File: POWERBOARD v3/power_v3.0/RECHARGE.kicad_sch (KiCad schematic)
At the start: 25 parts, among them J1 USB_C_Receptacle_USB2.0_16P, J2 B2B_PH_K_S, J3 R14 - 103AT-2, U2 BQ25886RGE

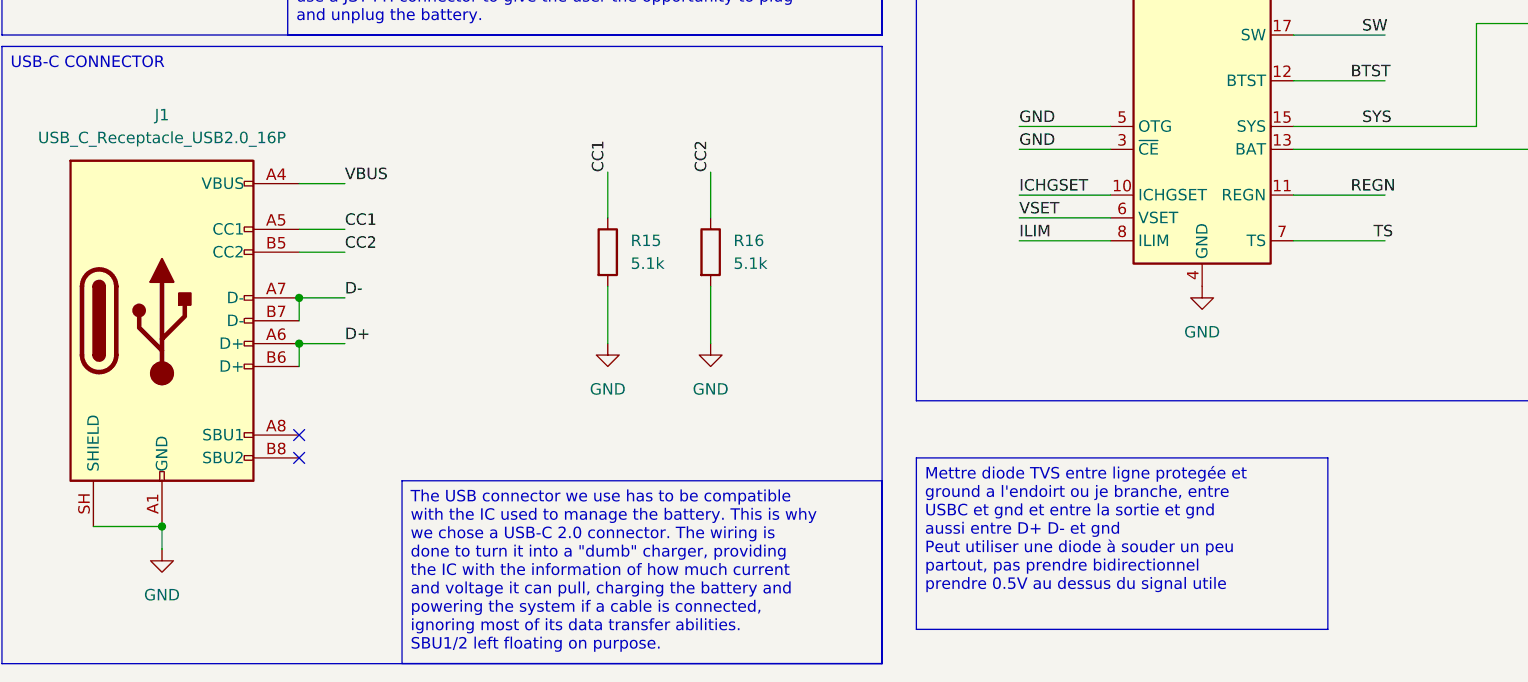
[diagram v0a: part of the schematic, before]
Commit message: added TVS diodes to charging circuit and (almost fully) routed 5.3 to 5V LDO
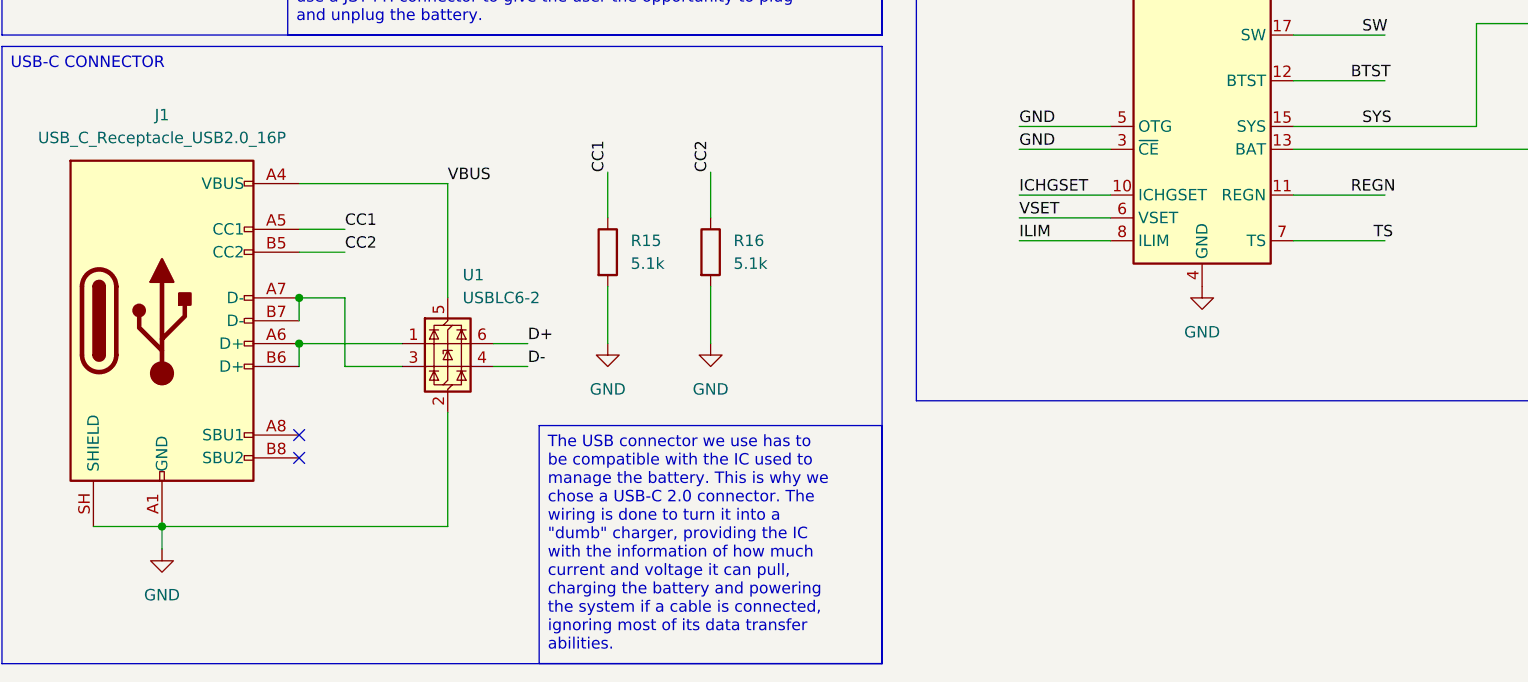
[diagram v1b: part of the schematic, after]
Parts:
- added U1: USBLC6-2, Package_TO_SOT_SMD:SOT-23-6, symbol Power_Protection:USBLC6-2SC6
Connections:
- net D+: now also U1.6 (I/O1); no longer J1.A6 (D+), J1.B6 (D+)
- net D-: now also U1.4 (I/O2); no longer J1.A7 (D-), J1.B7 (D-)
- net GND: now also U1.2 (GND)
- net VBUS: now also U1.5 (VBUS)
- new net: J1.A6 (D+), J1.B6 (D+), U1.1 (I/O1)
- new net: J1.A7 (D-), J1.B7 (D-), U1.3 (I/O2)
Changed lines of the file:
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@@
 		)
 	)
-	(text_box "Mettre diode TVS entre ligne protegée et ground a l'endoirt ou je branche, entre USBC et gnd et entre la sortie et gnd\naussi entre D+ D- et gnd\nPeut utiliser une diode à souder un peu partout, pas prendre bidirectionnel\nprendre 0.5V au dessus du signal utile"
-		(exclude_from_sim no)
-		(at 129.54 170.18 0)
-		(size 45.72 19.0501)
-		(margins 0.9525 0.9525 0.9525 0.9525)
-		(stroke
-			(width 0)
-			(type solid)
-		)
-		(fill
-			(type none)
-		)
-		(effects
-			(font
-				(size 1.27 1.27)
-			)
-			(justify left top)
-		)
-	)
 	(text_box "R14 is a thermistor to be placed as close to the battery as possible. The Seiko BMS integrated in our battery only handles the electric protection (charge, discharge) and not the temperature. Via TS, the IC progressively adjusts the charging profile according to the temperature to preserve the battery (JEITA). Its value at 25°C should be of 10kOhm."
 		(exclude_from_sim no)
@@
 		)
 	)
-	(text_box "The USB connector we use has to be compatible with the IC used to manage the battery. This is why we chose a USB-C 2.0 connector. The wiring is done to turn it into a \"dumb\" charger, providing the IC with the information of how much current and voltage it can pull, charging the battery and powering the system if a cable is connected, ignoring most of its data transfer abilities.\nSBU1/2 left floating on purpose."
+	(text_box "The USB connector we use has to be compatible with the IC used to manage the battery. This is why we chose a USB-C 2.0 connector. The wiring is done to turn it into a \"dumb\" charger, providing the IC with the information of how much current and voltage it can pull, charging the battery and powering the system if a cable is connected, ignoring most of its data transfer abilities."
 		(exclude_from_sim no)
-		(at 72.39 172.72 0)
-		(size 53.34 20.3053)
+		(at 87.63 166.5861 0)
+		(size 38.1 26.4392)
 		(margins 0.9525 0.9525 0.9525 0.9525)
 		(stroke
@@
 	(wire
 		(pts
+			(xy 82.55 157.48) (xy 86.36 157.48)
+		)
+		(stroke
+			(width 0)
+			(type default)
+		)
+	)
+	(wire
+		(pts
 			(xy 64.77 46.99) (xy 64.77 45.72)
 		)
@@
 	(wire
 		(pts
-			(xy 66.04 139.7) (xy 60.96 139.7)
+			(xy 60.96 139.7) (xy 77.47 139.7)
+		)
+		(stroke
+			(width 0)
+			(type default)
+		)
+	)
+	(wire
+		(pts
+			(xy 66.04 160.02) (xy 72.39 160.02)
 		)
 		(stroke
@@
 	(wire
 		(pts
-			(xy 60.96 157.48) (xy 66.04 157.48)
+			(xy 60.96 157.48) (xy 72.39 157.48)
 		)
 		(stroke
@@
 	(wire
 		(pts
+			(xy 82.55 160.02) (xy 86.36 160.02)
+		)
+		(stroke
+			(width 0)
+			(type default)
+		)
+	)
+	(wire
+		(pts
 			(xy 203.2 121.92) (xy 212.09 121.92)
 		)
@@
 	(wire
 		(pts
+			(xy 66.04 152.4) (xy 66.04 160.02)
+		)
+		(stroke
+			(width 0)
+			(type default)
+		)
+	)
+	(wire
+		(pts
 			(xy 191.77 133.35) (xy 171.45 133.35)
 		)
@@
 	(wire
 		(pts
+			(xy 77.47 139.7) (xy 77.47 152.4)
+		)
+		(stroke
+			(width 0)
+			(type default)
+		)
+	)
+	(wire
+		(pts
 			(xy 194.31 113.03) (xy 200.66 113.03)
 		)
@@
 	(wire
 		(pts
+			(xy 77.47 165.1) (xy 77.47 177.8)
+		)
+		(stroke
+			(width 0)
+			(type default)
+		)
+	)
+	(wire
+		(pts
 			(xy 115.57 34.29) (xy 115.57 43.18)
 		)
@@
 	(wire
 		(pts
+			(xy 77.47 177.8) (xy 45.72 177.8)
+		)
+		(stroke
+			(width 0)
+			(type default)
+		)
+	)
+	(wire
+		(pts
 			(xy 190.5 73.66) (xy 196.85 73.66)
 		)
@@
 	)
 	(label "VBUS"
-		(at 66.04 139.7 0)
+		(at 77.47 139.7 0)
 		(effects
 			(font
@@
 		)
 	)
-	(label "D-"
-		(at 66.04 152.4 0)
+	(label "ILIM"
+		(at 140.97 146.05 0)
 		(effects
 			(font
@@
 		)
 	)
-	(label "ILIM"
-		(at 140.97 146.05 0)
+	(label "REGN"
+		(at 196.85 49.53 90)
 		(effects
 			(font
@@
 		)
 	)
-	(label "REGN"
-		(at 196.85 49.53 90)
+	(label "D-"
+		(at 86.36 160.02 0)
 		(effects
 			(font
@@
 		)
 	)
-	(label "D+"
-		(at 66.04 157.48 0)
+	(label "ICHGSET"
+		(at 95.25 34.29 90)
 		(effects
 			(font
@@
 		)
 	)
-	(label "ICHGSET"
-		(at 95.25 34.29 90)
+	(label "RECHARGING_SYSTEM_"
+		(at 16.51 20.32 0)
 		(effects
 			(font
@@
 		)
 	)
-	(label "RECHARGING_SYSTEM_"
-		(at 16.51 20.32 0)
+	(label "D+"
+		(at 86.36 157.48 0)
 		(effects
 			(font
@@
 					(unit 1)
 				)
+			)
+		)
+	)
+	(symbol
+		(lib_id "Power_Protection:USBLC6-2SC6")
+		(at 77.47 157.48 0)
+		(unit 1)
+		(body_style 1)
+		(exclude_from_sim no)
+		(in_bom yes)
+		(on_board yes)
+		(in_pos_files yes)
+		(dnp no)
+		(fields_autoplaced yes)
+		(property "Reference" "U1"
+			(at 79.1211 149.86 0)
+			(show_name no)
+			(do_not_autoplace no)
+			(effects
+				(font
+					(size 1.27 1.27)
+				)
+				(justify left)
+			)
+		)
+		(property "Value" "USBLC6-2"
+			(at 79.1211 152.4 0)
+			(show_name no)
+			(do_not_autoplace no)
+			(effects
+				(font
+					(size 1.27 1.27)
+				)
+				(justify left)
+			)
+		)
+		(property "Footprint" "Package_TO_SOT_SMD:SOT-23-6"
+			(at 78.74 163.83 0)
+			(hide yes)
+			(show_name no)
+			(do_not_autoplace no)
+			(effects
+				(font
+					(size 1.27 1.27)
+					(italic yes)
+				)
+				(justify left)
+			)
+		)
+		(property "Datasheet" "https://www.st.com/resource/en/datasheet/usblc6-2.pdf"
+			(at 78.74 165.735 0)
+			(hide yes)
+			(show_name no)
+			(do_not_autoplace no)
+			(effects
+				(font
+					(size 1.27 1.27)
+				)
+				(justify left)
+			)
+		)
+		(property "Description" "Very low capacitance ESD protection diode, 2 data-line, SOT-23-6"
+			(at 77.47 157.48 0)
+			(hide yes)
+			(show_name no)
+			(do_not_autoplace no)
+			(effects
+				(font
+					(size 1.27 1.27)
+				)
+			)
+		)
+		(pin "5"
+		)
+		(pin "4"
+		)
+		(pin "6"
+		)
+		(pin "3"
+		)
+		(pin "2"
+		)
+		(pin "1"
+		)
+		(instances
+			(project "power_v3.0"
+				(path "/432bcdcf-747a-4fa0-b87b-096f44260199/b63164f7-da09-43bf-9854-ef6b4b4934c1"
+					(reference "U1")
+					(unit 1)
+				)

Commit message: Fixed diode layout, added C to VBUS and protection to BUCK-LDO interface
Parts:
- added C12: 22u, symbol Device:C
- L2: footprint Inductor_SMD:L_0805_2012Metric -> (none)
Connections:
- net GND: now also C12.2
- net VBUS: now also C12.1
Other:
- moved on the sheet: C1, C2, C3, L2, R1, R2, R9
